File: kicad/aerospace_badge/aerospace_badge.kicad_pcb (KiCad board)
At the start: 2 copper layers, 134.3 x 140 mm, 20 parts, among them J1 Conn_01x02, J2 Conn_01x02, J3 Conn_02x03_Counter_Clockwise, J4 Conn_01x04, J6 Conn_01x01_Male, J7 Conn_01x01_Male, J8 Conn_01x01_Male, SW1 SW_SPDT, U1 ATtiny85-20SU

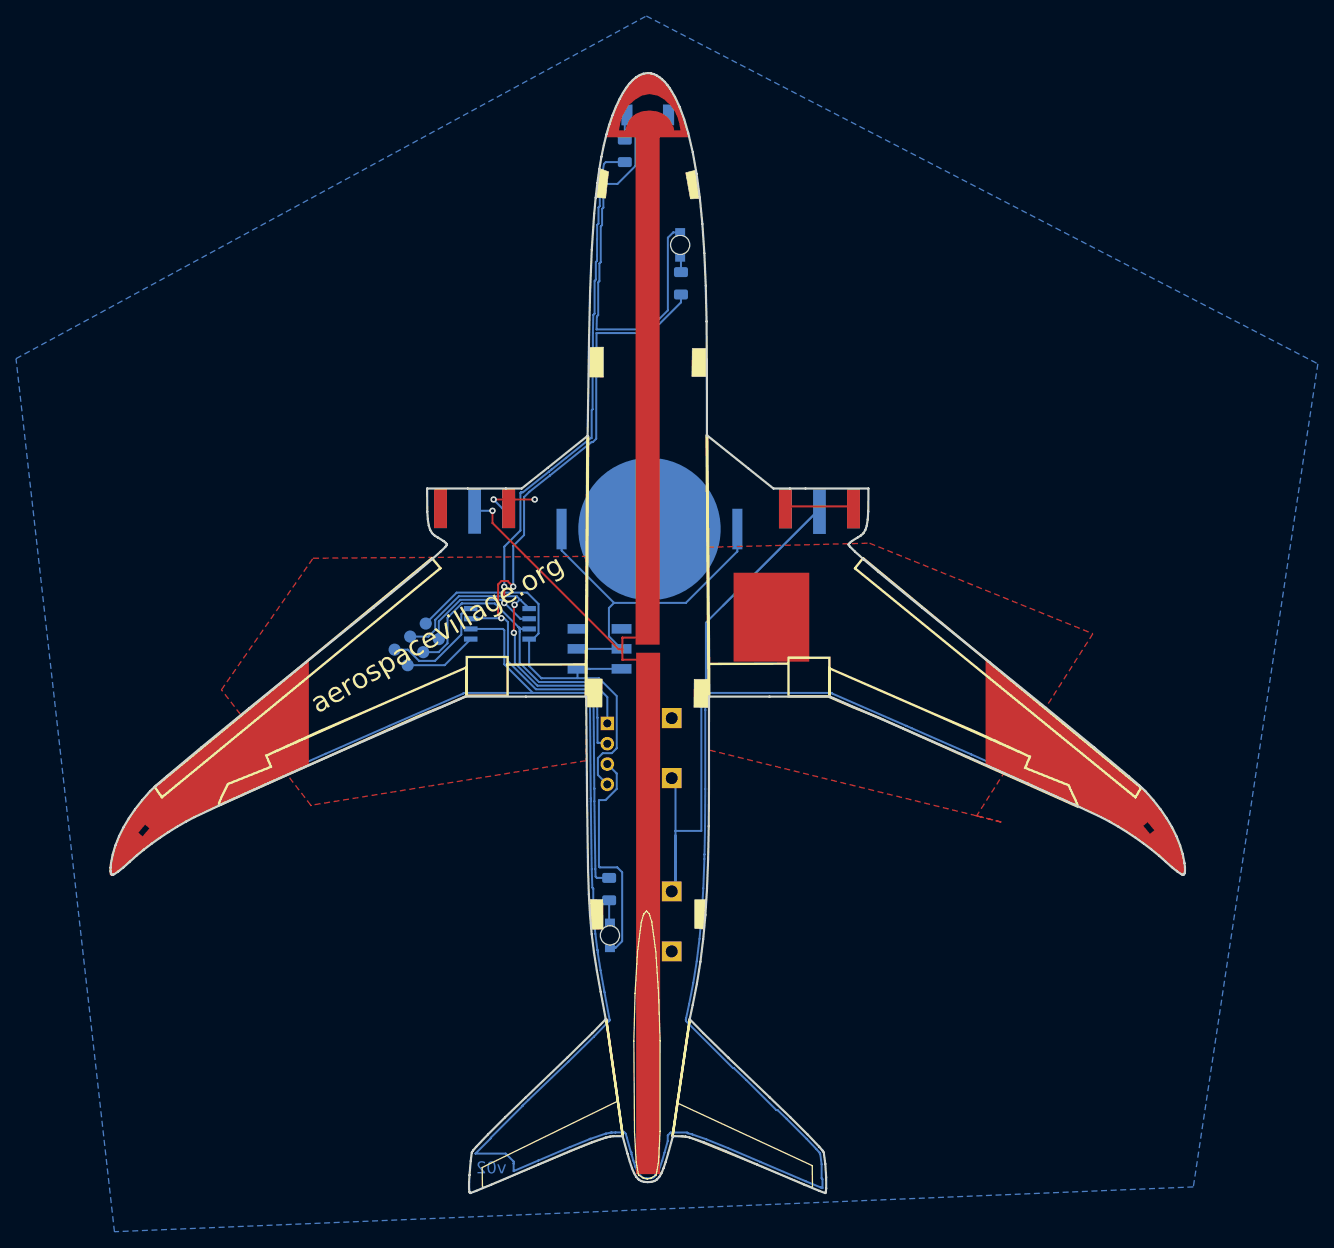
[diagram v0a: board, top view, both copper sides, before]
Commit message: jlcpcb rejected because traces too close to edge, trace refactor.
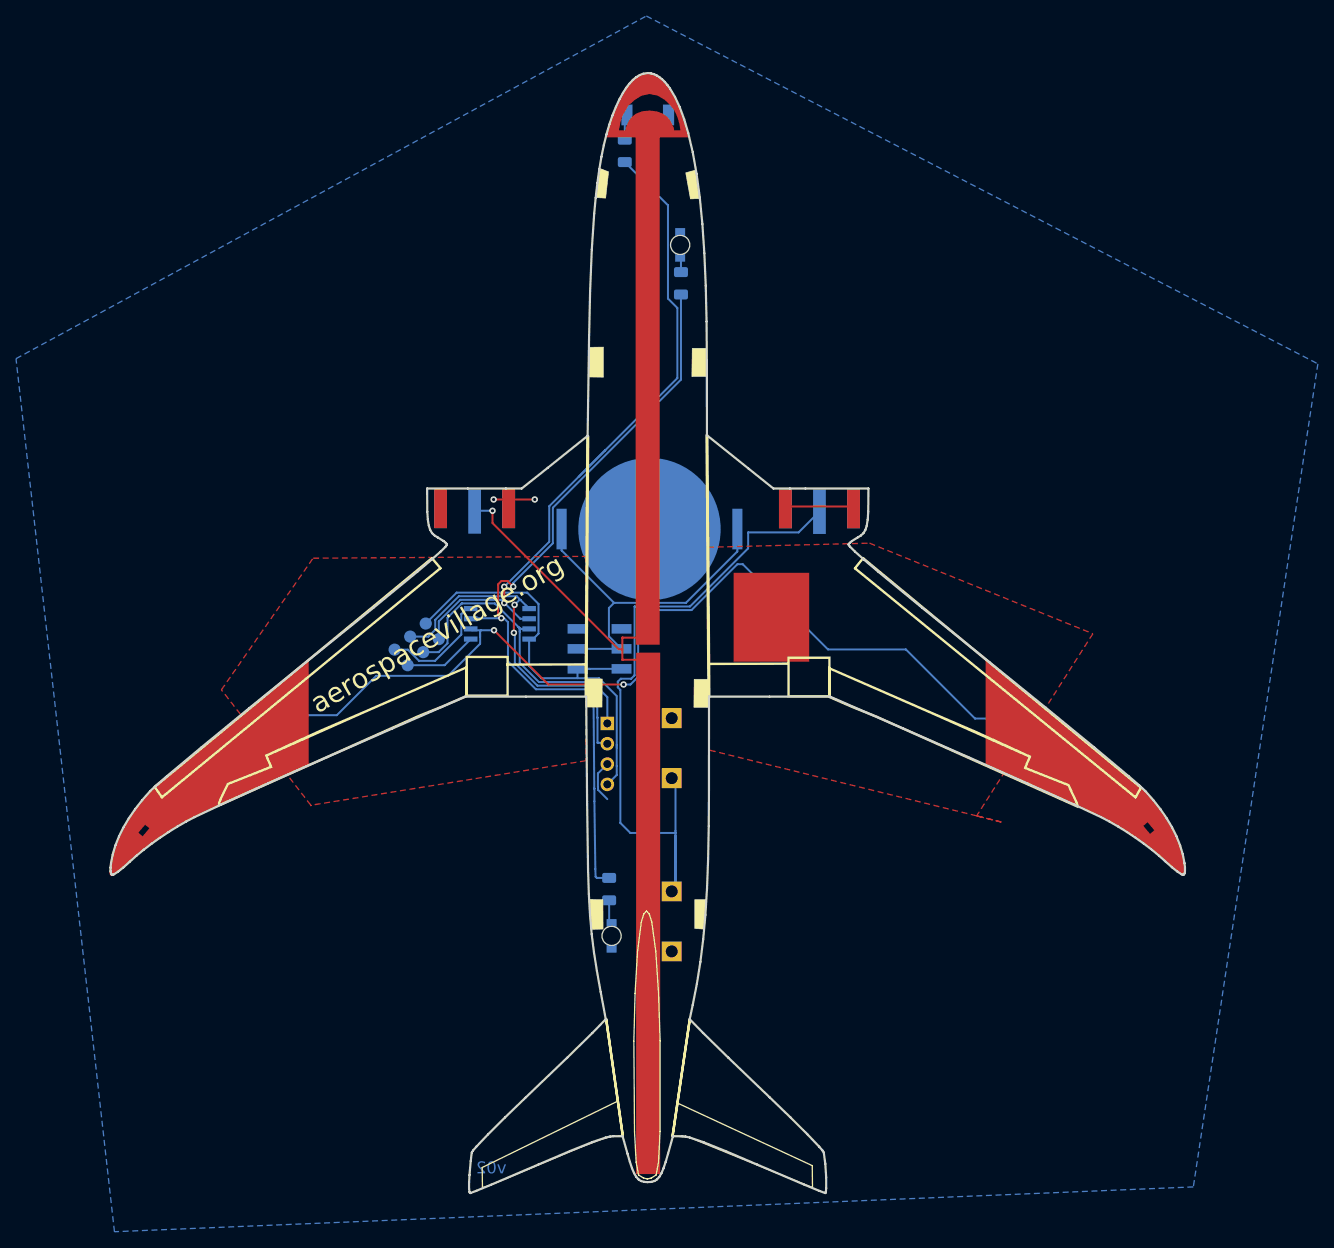
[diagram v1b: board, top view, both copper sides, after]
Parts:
- moved R3 0.74 mm to (92.4, 110.4), turned to 220 degrees
- moved R2 0.69 mm to (204.8, 110.7), turned to 320 degrees
- moved D4 0.21 mm to (143.9, 129.3)
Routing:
- net Net-(R2-Pad1): track 303.9 -> 147.8 mm, vias 0 -> 2
- net GND: track 128.3 -> 48.8 mm
- net Net-(J3-Pad1): track 79.2 -> 87.2 mm
- net Net-(R4-Pad1): track 103.7 -> 99.1 mm
- net Net-(J2-Pad1): track 87.7 -> 86.5 mm
- net VCC: track 58.7 -> 57.5 mm
- net Net-(D3-Pad2): track 4.88 -> 4.19 mm
- net Net-(D2-Pad2): track 4.35 -> 3.75 mm

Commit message: cosmetic updates and KiCad version update, footprint inclusions
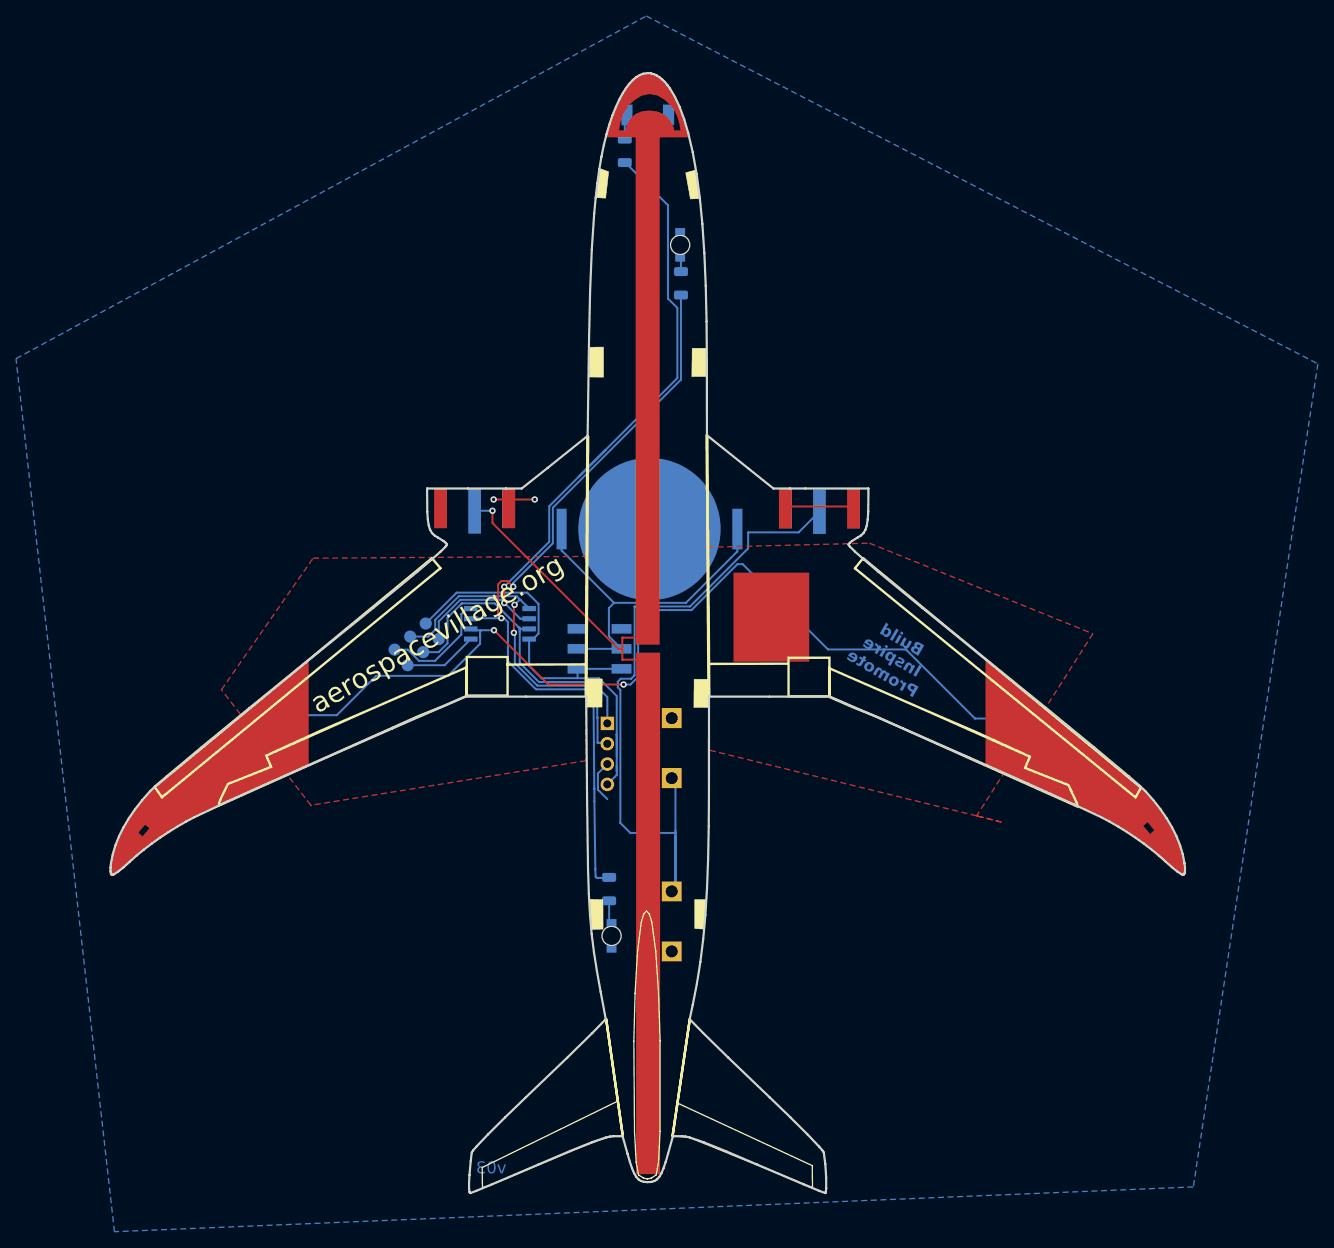
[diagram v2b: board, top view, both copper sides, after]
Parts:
- R1, R2, R3, R4, R5: footprint Resistors_SMD:R_1206_3216Metric -> Resistor_SMD:R_1206_3216Metric
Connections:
- SW1 pad 1: Net-(SW1-Pad1) -> unconnected-(SW1-A-Pad1)
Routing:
- net VCC: track 57.5 -> 58.8 mm
- added copper zone on F.Cu, net GND
- removed copper zone on F.Cu, net (none)
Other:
- net class Default removed
- board text added: "Build Inspire Promote"
- board text added: "v03"
- board text removed: "captechu.edu"
- board text removed: "v02"
